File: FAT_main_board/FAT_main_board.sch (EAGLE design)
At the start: 27 parts, among them IC1 74LS241N

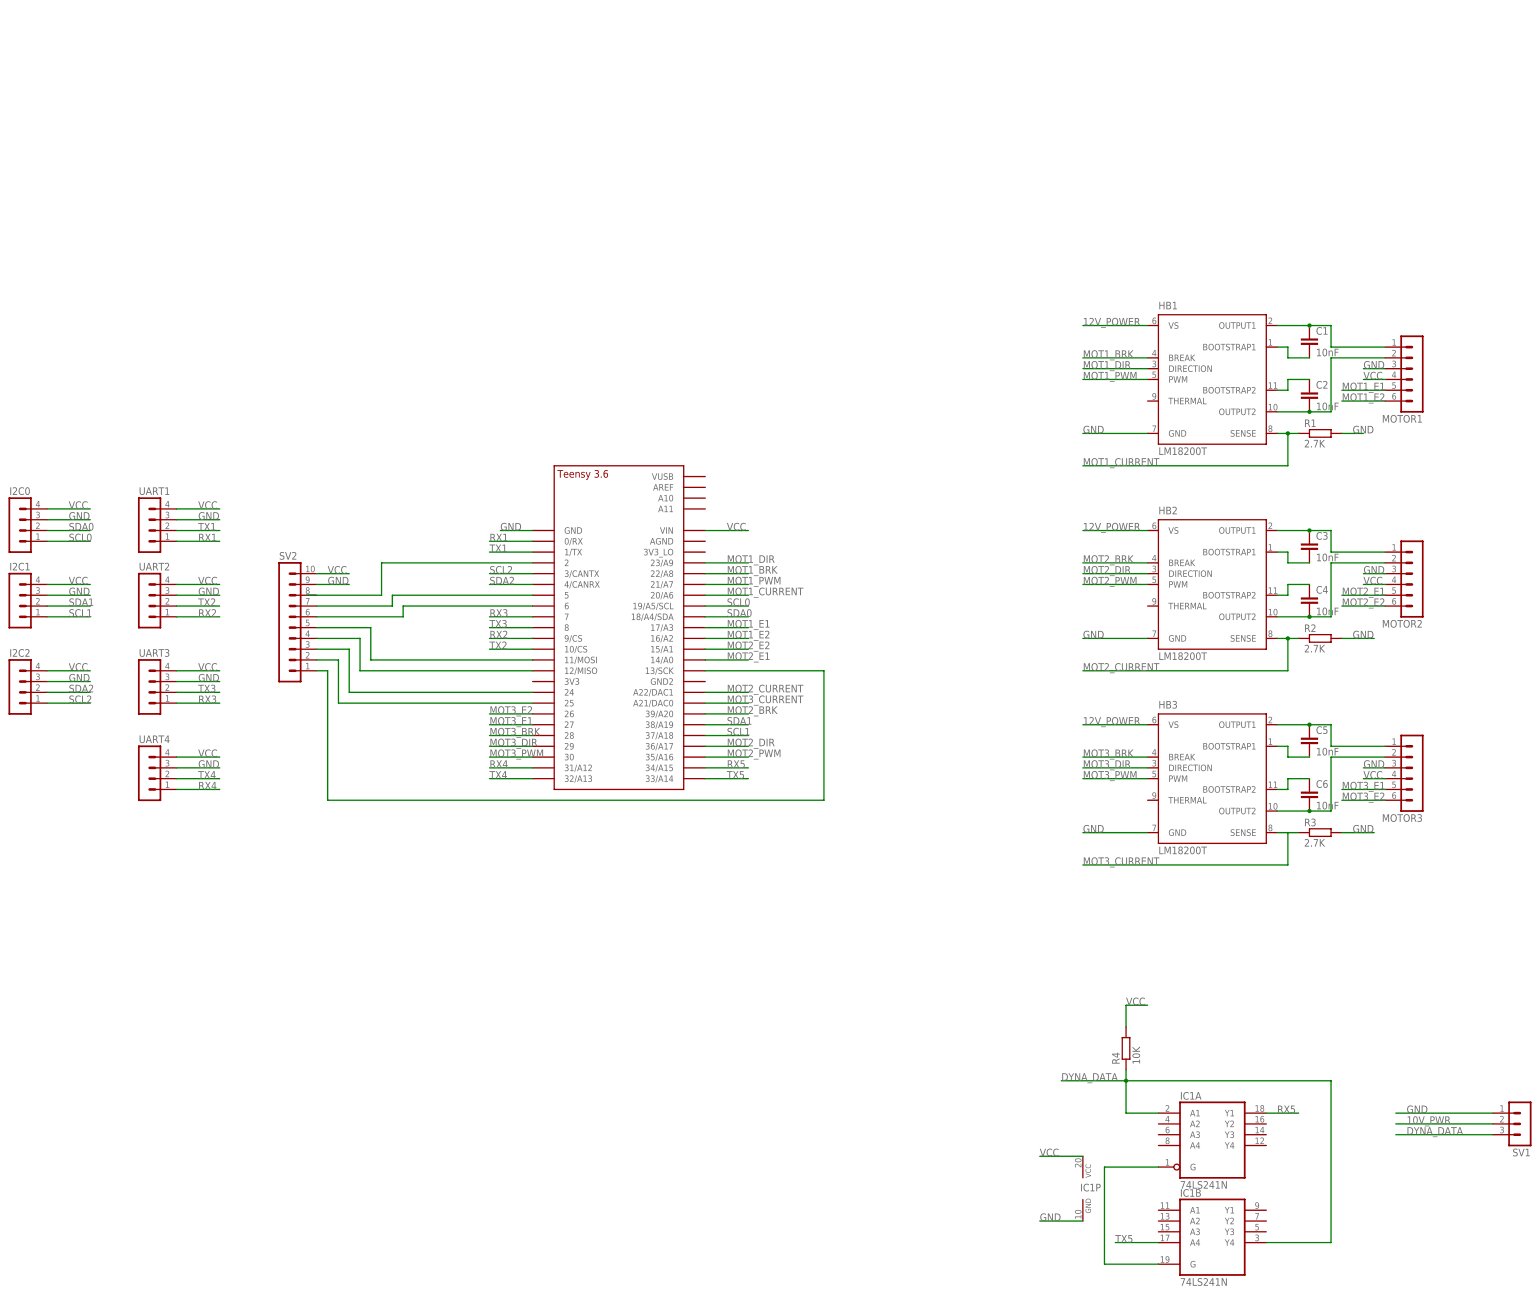
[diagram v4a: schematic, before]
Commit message: [FAT board] Adds power supply.
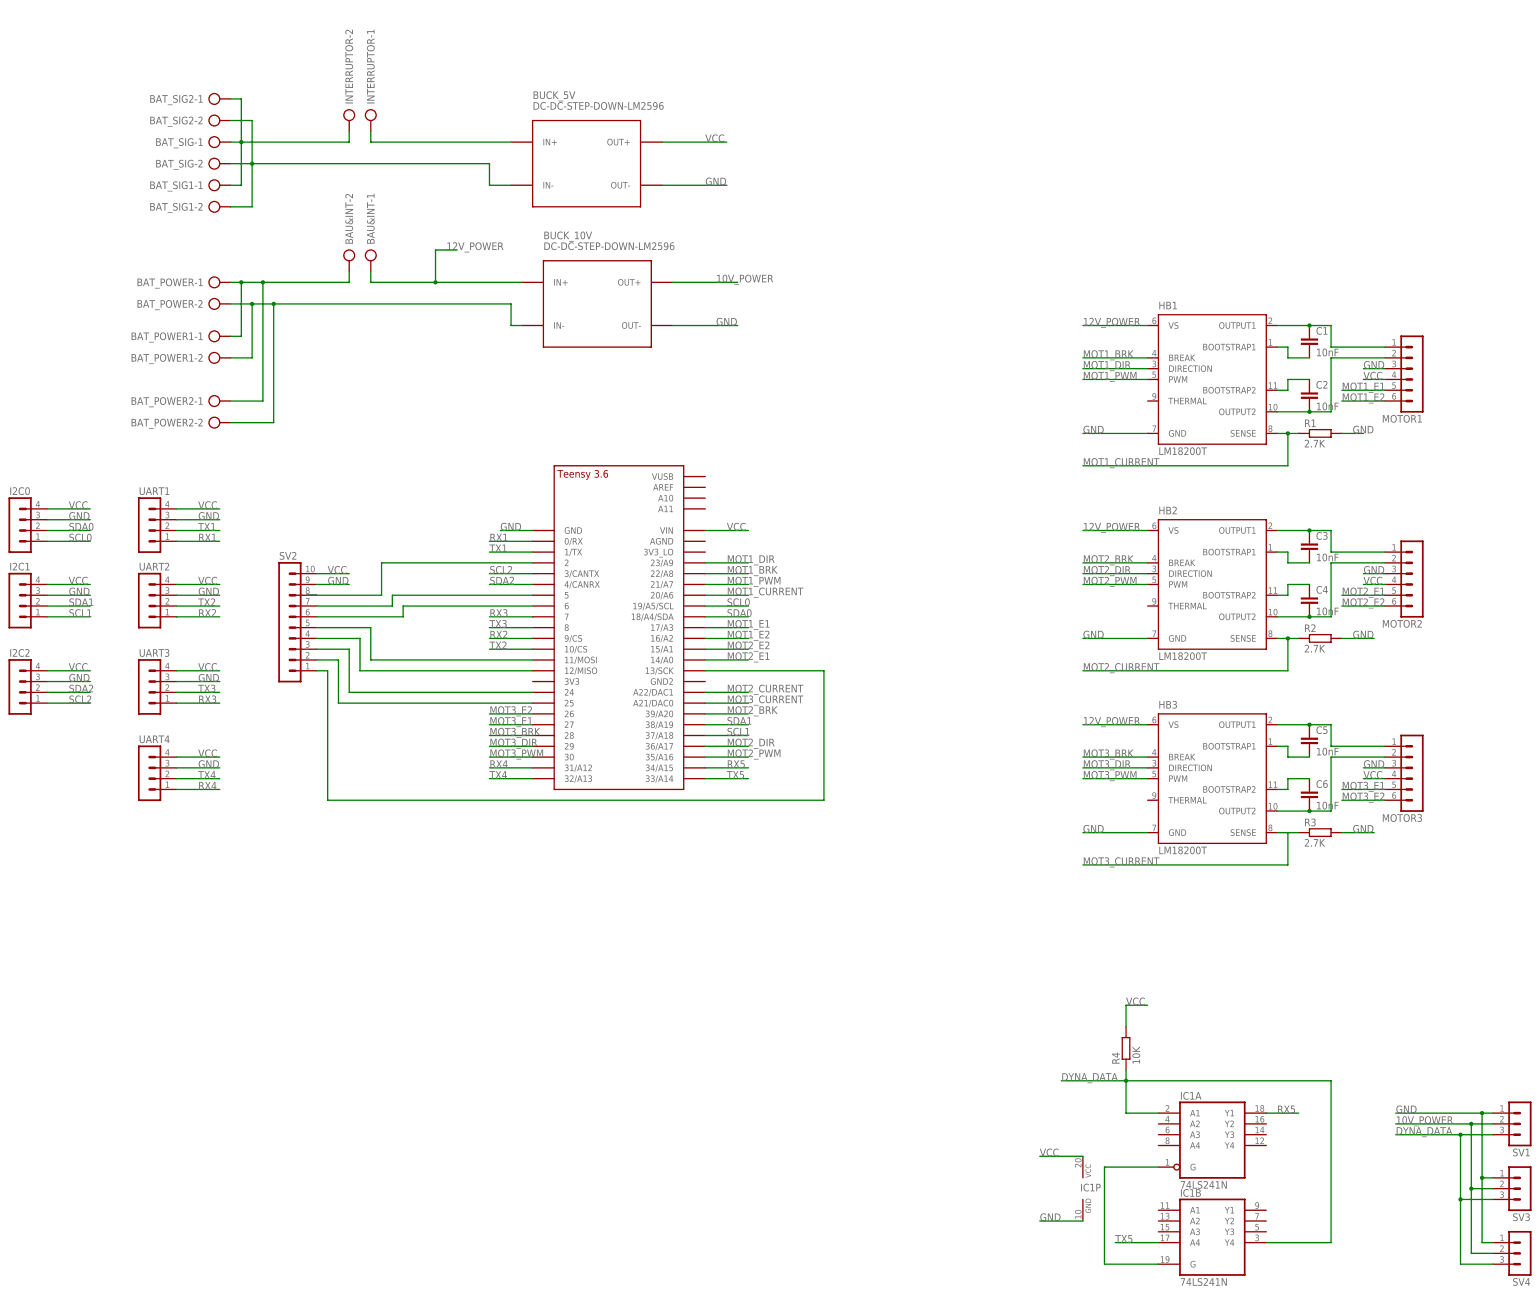
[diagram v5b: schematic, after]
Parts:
- added BAT_POWER, BAT_POWER1, BAT_POWER2, BAT_SIG, BAT_SIG1, BAT_SIG2, BAU&INT, INTERRUPTOR: (no value), con-ptr500:AK300/2
- added BUCK_10V, BUCK_5V: DC-DC-STEP-DOWN-LM2596, diy-modules:DC-DC-STEP-DOWN-LM2596
- added SV3, SV4: (no value), con-lstb:MA03-1
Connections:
- removed net 10V_PWR: SV1.2
- new net 10V_POWER: BUCK_10V.OUT+, SV1.2, SV3.2, SV4.2
- new net N$13: BAT_POWER-1.KL, BAT_POWER1-1.KL, BAT_POWER2-1.KL, BAU&INT-2.KL
- new net N$20: BAT_SIG-1.KL, BAT_SIG1-1.KL, BAT_SIG2-1.KL, INTERRUPTOR-2.KL
- new net N$22: BUCK_5V.IN+, INTERRUPTOR-1.KL
- new net N$23: BAT_POWER-2.KL, BAT_POWER1-2.KL, BAT_POWER2-2.KL, BUCK_10V.IN-
- new net N$25: BAT_SIG-2.KL, BAT_SIG1-2.KL, BAT_SIG2-2.KL, BUCK_5V.IN-
- net 12V_POWER: now also BAU&INT-1.KL, BUCK_10V.IN+
- net DYNA_DATA: now also SV3.3, SV4.3
- net GND: now also BUCK_10V.OUT-, BUCK_5V.OUT-, SV3.1, SV4.1
- net VCC: now also BUCK_5V.OUT+

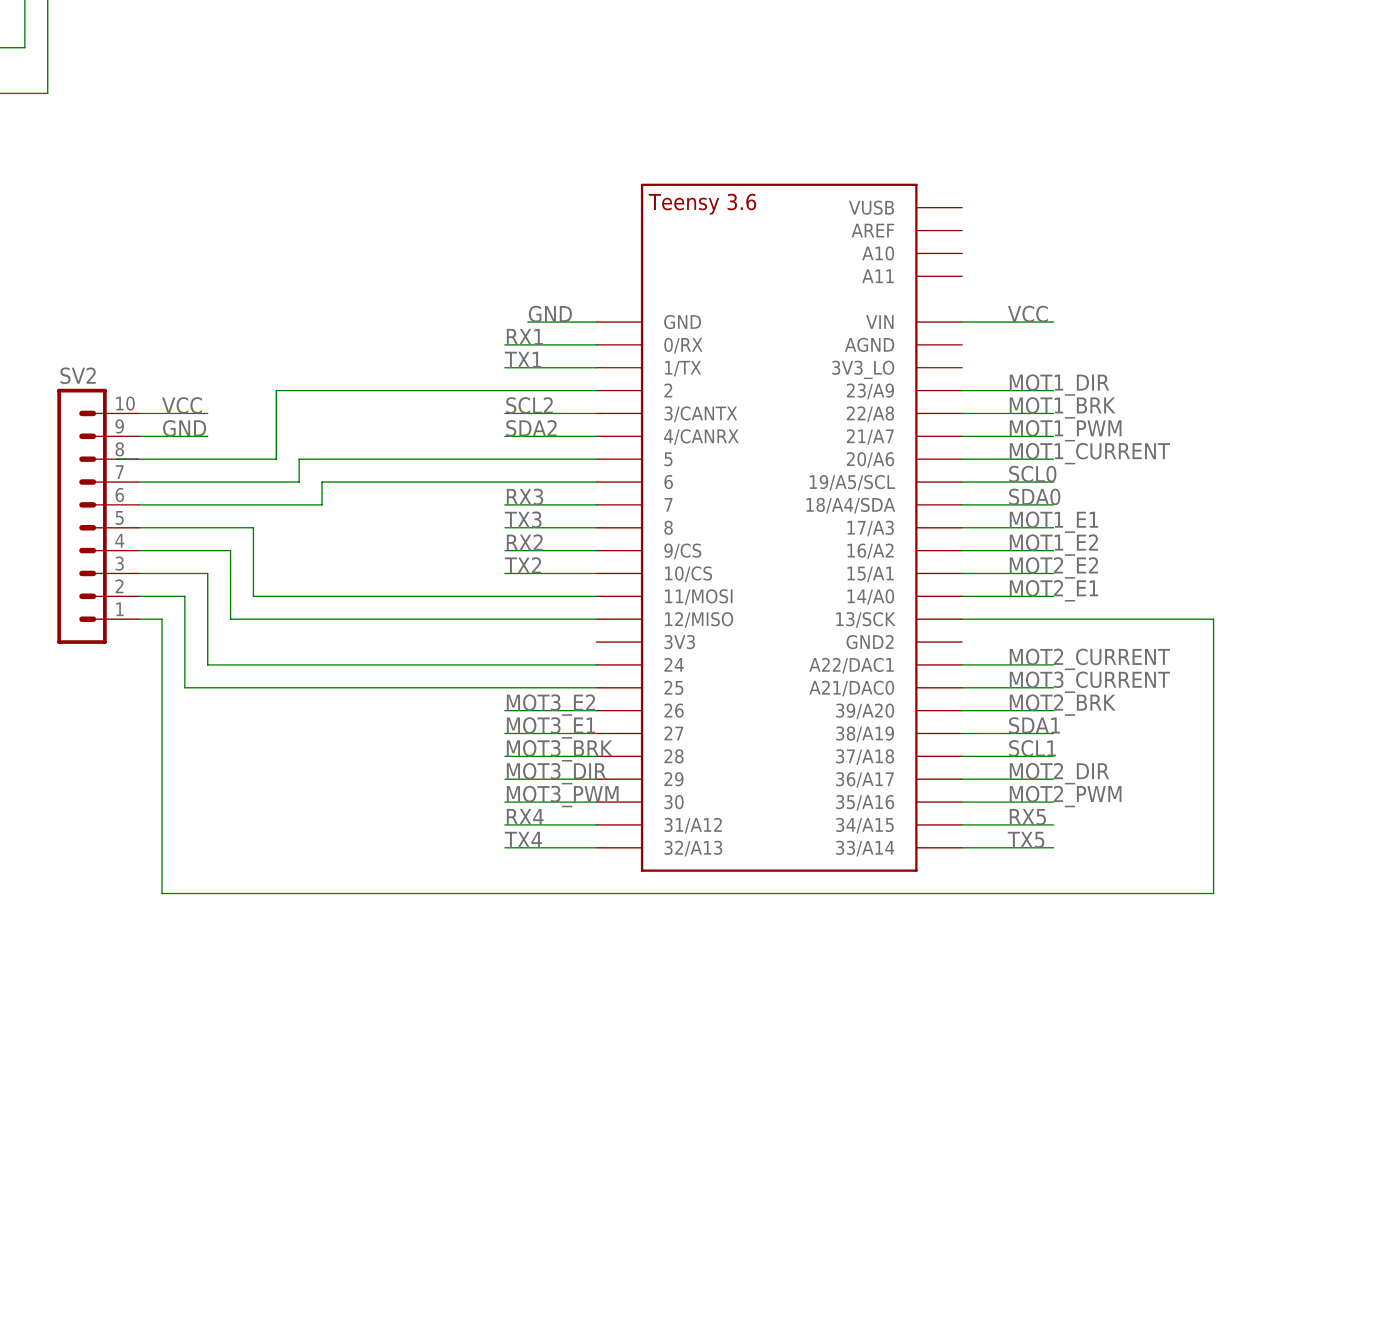
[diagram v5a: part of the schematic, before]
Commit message: [FAT board] Adds reset button.
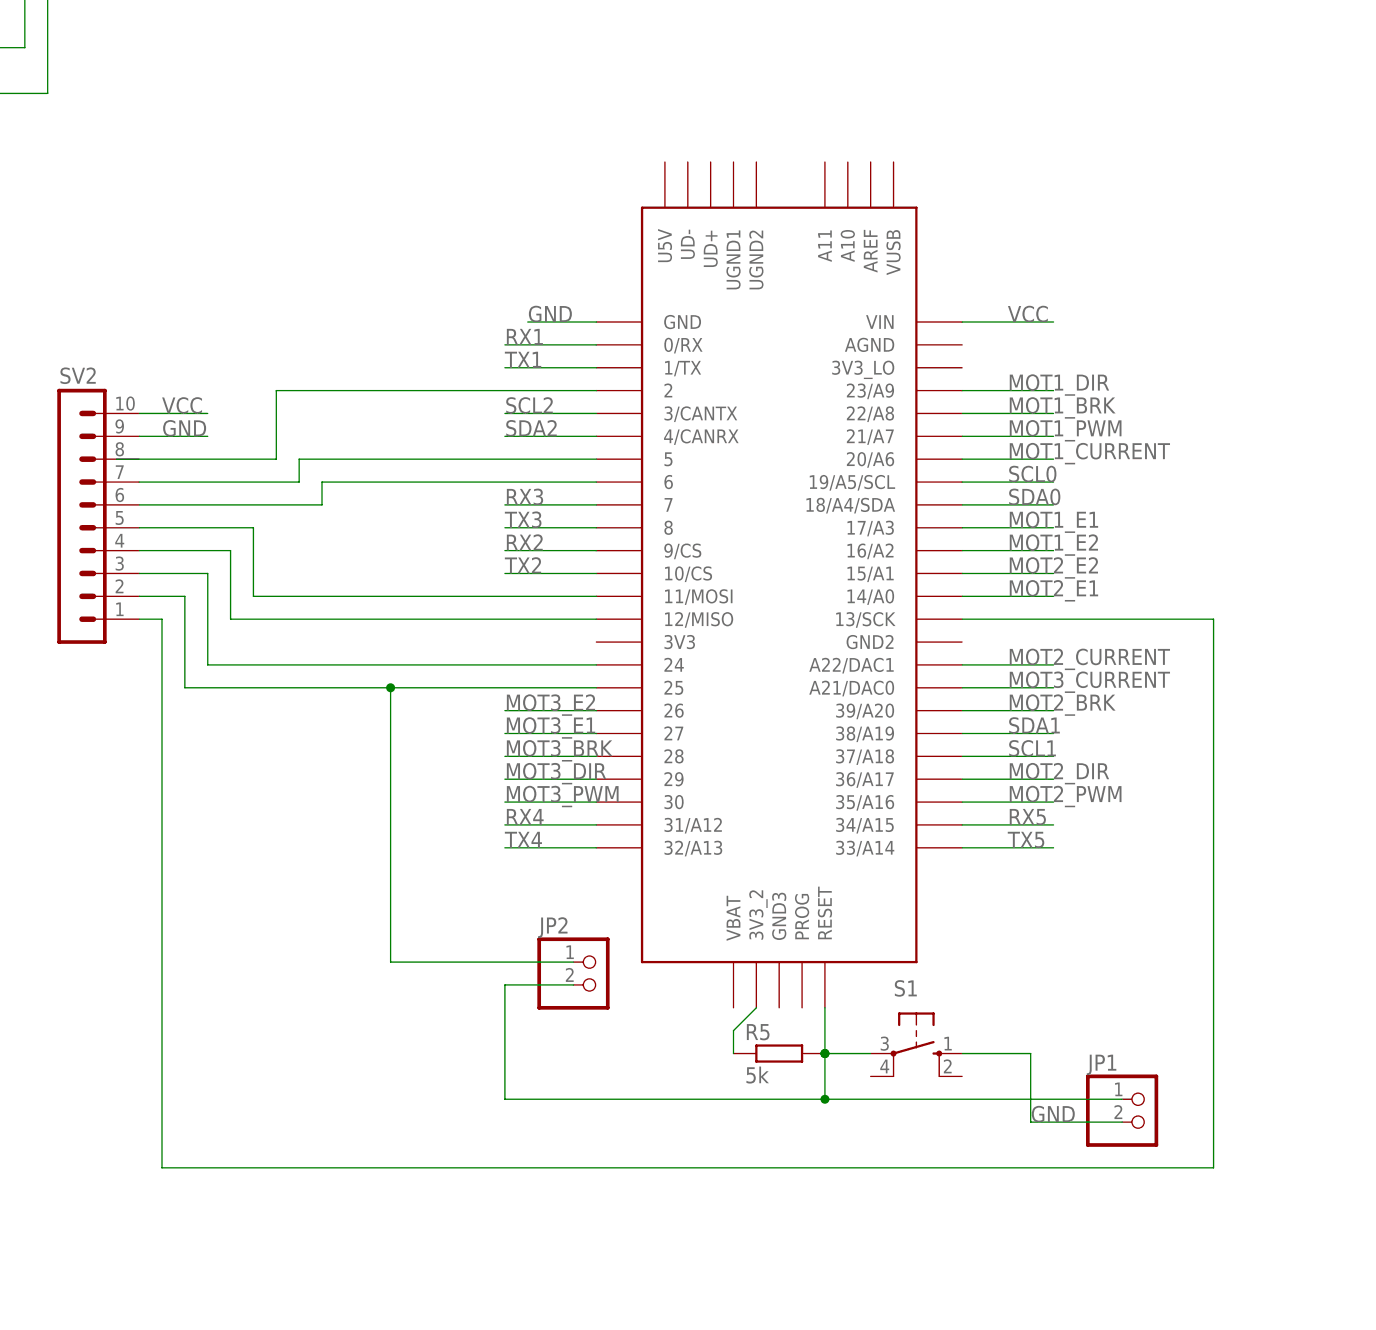
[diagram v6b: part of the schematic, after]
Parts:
- added JP1, JP2: (no value), pinhead:PINHD-1X2
- added R5: 5k, rcl:R-EU_0204/7
- added S1: (no value), switch-omron:10-XX
- U$1: value TEENSY_3.5/3.6_BASIC -> TEENSY_3.5/3.6; device Teensy356:TEENSY_3.5/3.6_BASIC -> Teensy356:TEENSY_3.5/3.6
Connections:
- new net N$19: JP1.1, JP2.2, R5.2, S1.P, U$1.RESET
- new net N$26: R5.1, U$1.3V3_2
- net GND: now also JP1.2, S1.S
- net N$40: now also JP2.1
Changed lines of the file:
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@@
 <part name="HB2" library="national-semiconductor" deviceset="LM18200T" device=""/>
 <part name="HB3" library="national-semiconductor" deviceset="LM18200T" device=""/>
-<part name="U$1" library="Teensy356" deviceset="TEENSY_3.5/3.6_BASIC" device=""/>
+<part name="U$1" library="Teensy356" deviceset="TEENSY_3.5/3.6" device=""/>
 <part name="MOTOR1" library="con-lstb" deviceset="MA06-1" device=""/>
 <part name="MOTOR2" library="con-lstb" deviceset="MA06-1" device=""/>
@@
 <part name="SV3" library="con-lstb" deviceset="MA03-1" device=""/>
 <part name="SV4" library="con-lstb" deviceset="MA03-1" device=""/>
+<part name="JP1" library="pinhead" deviceset="PINHD-1X2" device=""/>
+<part name="R5" library="rcl" deviceset="R-EU_" device="0204/7" value="5k"/>
+<part name="S1" library="switch-omron" deviceset="10-XX" device=""/>
+<part name="JP2" library="pinhead" deviceset="PINHD-1X2" device=""/>
 </parts>
 <sheets>
@@
 <instance part="SV3" gate="G$1" x="213.36" y="-132.08" rot="R180"/>
 <instance part="SV4" gate="G$1" x="213.36" y="-147.32" rot="R180"/>
+<instance part="JP1" gate="G$1" x="40.64" y="-66.04"/>
+<instance part="R5" gate="G$1" x="0" y="-58.42"/>
+<instance part="S1" gate="1" x="15.24" y="-58.42" rot="R270"/>
+<instance part="JP2" gate="G$1" x="-20.32" y="-50.8"/>
 </instances>
 <busses>
@@
 <label x="20.32" y="104.14" size="1.778" layer="95"/>
 </segment>
+<segment>
+<pinref part="JP1" gate="G$1" pin="2"/>
+<wire x1="38.1" y1="-66.04" x2="27.94" y2="-66.04" width="0.1524" layer="91"/>
+<label x="27.94" y="-66.04" size="1.778" layer="95"/>
+<pinref part="S1" gate="1" pin="S"/>
+<wire x1="20.32" y1="-58.42" x2="27.94" y2="-58.42" width="0.1524" layer="91"/>
+<wire x1="27.94" y1="-58.42" x2="27.94" y2="-66.04" width="0.1524" layer="91"/>
+</segment>
 </net>
 <net name="VCC" class="0">
@@
 <wire x1="-71.12" y1="-7.62" x2="-66.04" y2="-7.62" width="0.1524" layer="91"/>
 <wire x1="-66.04" y1="-7.62" x2="-66.04" y2="-17.78" width="0.1524" layer="91"/>
-<wire x1="-66.04" y1="-17.78" x2="-20.32" y2="-17.78" width="0.1524" layer="91"/>
+<wire x1="-66.04" y1="-17.78" x2="-43.18" y2="-17.78" width="0.1524" layer="91"/>
+<wire x1="-43.18" y1="-17.78" x2="-20.32" y2="-17.78" width="0.1524" layer="91"/>
+<wire x1="-43.18" y1="-17.78" x2="-43.18" y2="-48.26" width="0.1524" layer="91"/>
+<junction x="-43.18" y="-17.78"/>
+<pinref part="JP2" gate="G$1" pin="1"/>
+<wire x1="-43.18" y1="-48.26" x2="-22.86" y2="-48.26" width="0.1524" layer="91"/>
 </segment>
 </net>
@@
 <pinref part="U$1" gate="G$1" pin="13/SCK"/>
 <wire x1="20.32" y1="-10.16" x2="48.26" y2="-10.16" width="0.1524" layer="91"/>
-<wire x1="48.26" y1="-10.16" x2="48.26" y2="-40.64" width="0.1524" layer="91"/>
-<wire x1="48.26" y1="-40.64" x2="-68.58" y2="-40.64" width="0.1524" layer="91"/>
-<wire x1="-68.58" y1="-40.64" x2="-68.58" y2="-10.16" width="0.1524" layer="91"/>
+<wire x1="48.26" y1="-10.16" x2="48.26" y2="-71.12" width="0.1524" layer="91"/>
+<wire x1="48.26" y1="-71.12" x2="-68.58" y2="-71.12" width="0.1524" layer="91"/>
+<wire x1="-68.58" y1="-71.12" x2="-68.58" y2="-10.16" width="0.1524" layer="91"/>
 <pinref part="SV2" gate="1" pin="1"/>
 <wire x1="-68.58" y1="-10.16" x2="-71.12" y2="-10.16" width="0.1524" layer="91"/>
@@
 </segment>
 </net>
+<net name="N$19" class="0">
+<segment>
+<pinref part="U$1" gate="G$1" pin="RESET"/>
+<wire x1="5.08" y1="-53.34" x2="5.08" y2="-58.42" width="0.1524" layer="91"/>
+<junction x="5.08" y="-58.42"/>
+<pinref part="JP1" gate="G$1" pin="1"/>
+<wire x1="5.08" y1="-58.42" x2="5.08" y2="-63.5" width="0.1524" layer="91"/>
+<wire x1="5.08" y1="-63.5" x2="38.1" y2="-63.5" width="0.1524" layer="91"/>
+<pinref part="R5" gate="G$1" pin="2"/>
+<junction x="5.08" y="-58.42"/>
+<wire x1="5.08" y1="-58.42" x2="10.16" y2="-58.42" width="0.1524" layer="91"/>
+<pinref part="S1" gate="1" pin="P"/>
+<pinref part="JP2" gate="G$1" pin="2"/>
+<wire x1="-22.86" y1="-50.8" x2="-30.48" y2="-50.8" width="0.1524" layer="91"/>
+<wire x1="-30.48" y1="-50.8" x2="-30.48" y2="-63.5" width="0.1524" layer="91"/>
+<wire x1="-30.48" y1="-63.5" x2="5.08" y2="-63.5" width="0.1524" layer="91"/>
+<junction x="5.08" y="-63.5"/>
+</segment>
+</net>
+<net name="N$26" class="0">
+<segment>
+<pinref part="U$1" gate="G$1" pin="3V3_2"/>
+<wire x1="-2.54" y1="-53.34" x2="-5.08" y2="-55.88" width="0.1524" layer="91"/>
+<pinref part="R5" gate="G$1" pin="1"/>
+<wire x1="-5.08" y1="-55.88" x2="-5.08" y2="-58.42" width="0.1524" layer="91"/>
+</segment>
+</net>
